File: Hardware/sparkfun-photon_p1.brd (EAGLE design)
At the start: 68.6 x 53.3 mm, 44 parts, among them U1 WM-N-BM-14

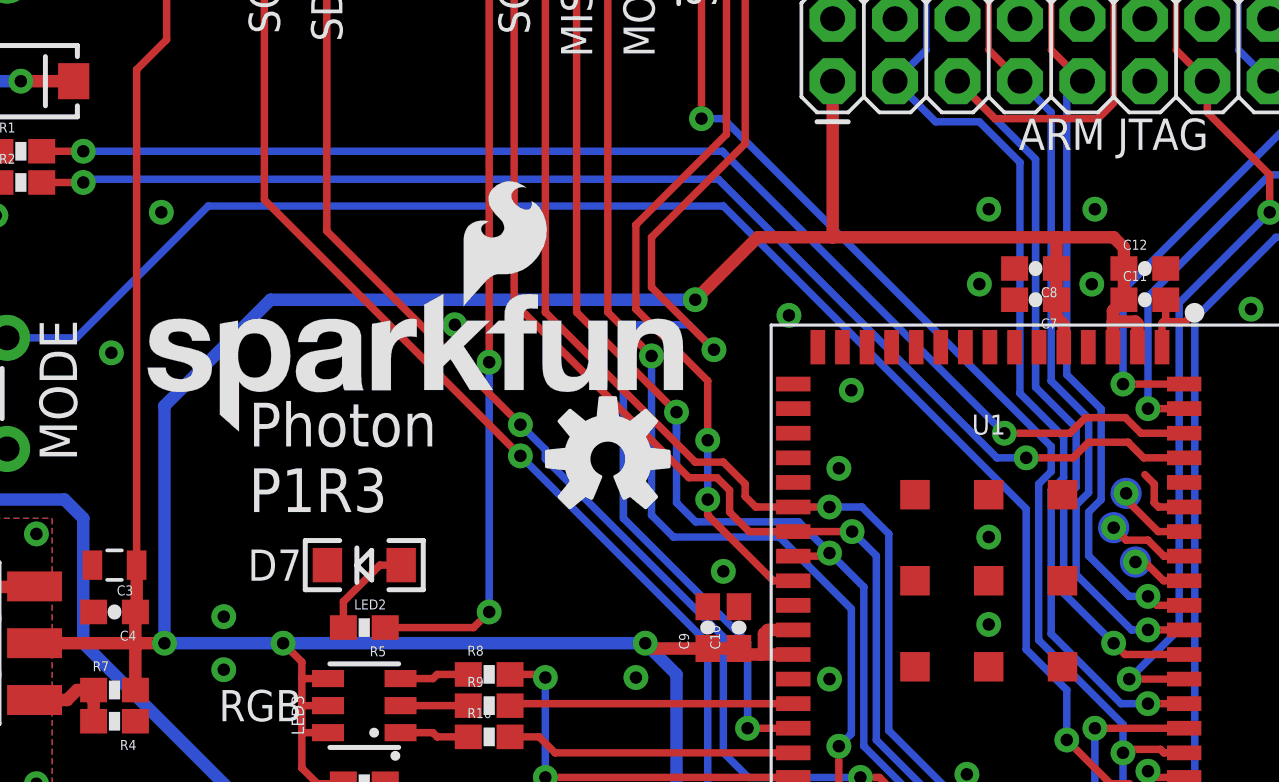
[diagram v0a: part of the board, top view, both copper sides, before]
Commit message: Moving a few vias for a more complete ground plane. Adjusting some silk.
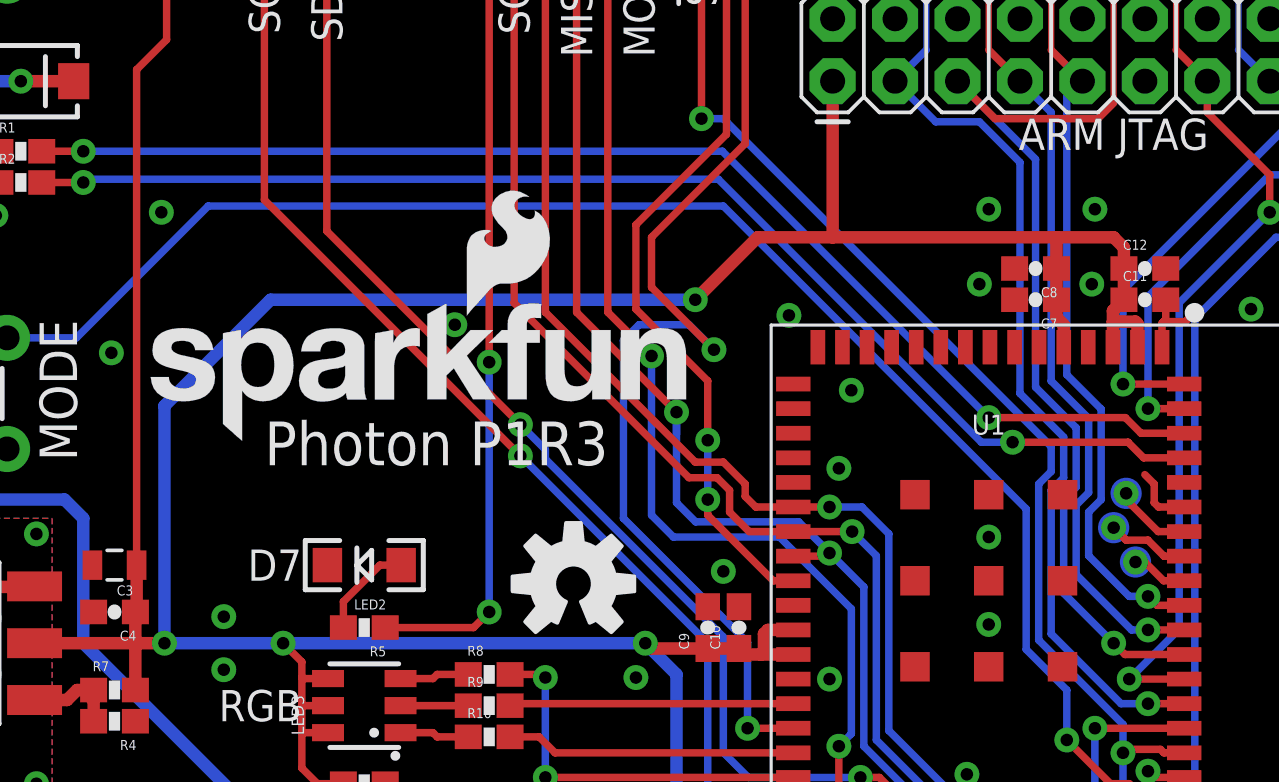
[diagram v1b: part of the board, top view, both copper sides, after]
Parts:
- moved LOGO1 5.27 mm to (31.4, 21.5)
- moved LOGO2 0.40 mm to (13.5, 27.2)
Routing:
- net MCU_USB_D-: track 51.7 -> 51.2 mm
- net MCU_USB_D+: track 51.7 -> 51.2 mm
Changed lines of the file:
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@@
 <layer number="47" name="Measures" color="7" fill="1" visible="no" active="yes"/>
 <layer number="48" name="Document" color="7" fill="1" visible="no" active="yes"/>
-<layer number="49" name="Reference" color="7" fill="1" visible="yes" active="yes"/>
+<layer number="49" name="Reference" color="7" fill="1" visible="no" active="yes"/>
 <layer number="50" name="dxf" color="7" fill="1" visible="no" active="no"/>
 <layer number="51" name="tDocu" color="6" fill="1" visible="yes" active="yes"/>
@@
 <text x="20.32" y="22.225" size="1.27" layer="21" font="vector" ratio="15" rot="R180" align="center-left">D7</text>
 <text x="20.32" y="10.795" size="1.27" layer="21" font="vector" ratio="15" rot="R180" align="center-left">POWER</text>
-<text x="18.161" y="28.829" size="1.778" layer="21" font="vector" ratio="15" align="top-left">Photon
-P1R3</text>
+<text x="18.796" y="28.067" size="1.778" layer="21" font="vector" ratio="15" align="top-left">Photon P1R3</text>
 <text x="9.652" y="29.337" size="1.524" layer="21" font="vector" ratio="15" rot="R90" align="top-center">MODE</text>
 <text x="9.652" y="48.387" size="1.524" layer="21" font="vector" ratio="15" rot="R90" align="top-center">RESET</text>
@@
 <attribute name="PROD_ID" value="CAP-00810" x="54.61" y="34.29" size="1.778" layer="27" font="vector" ratio="15" display="off"/>
 </element>
-<element name="LOGO2" library="SparkFun-Aesthetics" package="SFE_LOGO_NAME_FLAME_.2" value="SFE_LOGO_NAME_FLAME.2_INCH" x="13.335" y="27.559"/>
-<element name="LOGO1" library="SparkFun-Aesthetics" package="OSHW-LOGO-M" value="OSHW-LOGOM" x="32.766" y="26.543"/>
+<element name="LOGO2" library="SparkFun-Aesthetics" package="SFE_LOGO_NAME_FLAME_.2" value="SFE_LOGO_NAME_FLAME.2_INCH" x="13.462" y="27.178"/>
+<element name="LOGO1" library="SparkFun-Aesthetics" package="OSHW-LOGO-M" value="OSHW-LOGOM" x="31.369" y="21.463"/>
 <element name="U1" library="sparkfun_photon_temp" package="WM-N-BM-14" value="WM-N-BM-14" x="48.26" y="21.59">
 <attribute name="PROD_ID" value="IC-12589" x="48.26" y="21.59" size="1.778" layer="27" font="vector" ratio="15" display="off"/>
@@
 <wire x1="9.74" y1="39.06" x2="11.43" y2="39.06" width="0.3048" layer="1"/>
 <via x="11.43" y="39.06" extent="1-16" drill="0.508"/>
-<via x="48.895" y="27.59" extent="1-16" drill="0.508"/>
+<via x="48.26" y="28.225" extent="1-16" drill="0.508"/>
 <wire x1="11.43" y1="39.06" x2="37.425" y2="39.06" width="0.3048" layer="16"/>
-<wire x1="48.895" y1="27.59" x2="37.425" y2="39.06" width="0.3048" layer="16"/>
+<wire x1="48.26" y1="28.225" x2="37.425" y2="39.06" width="0.3048" layer="16"/>
 <wire x1="56.21" y1="27.59" x2="54.452" y2="27.59" width="0.3048" layer="1"/>
 <wire x1="54.452" y1="27.59" x2="53.817" y2="28.225" width="0.3048" layer="1"/>
-<wire x1="53.817" y1="28.225" x2="52.197" y2="28.225" width="0.3048" layer="1"/>
-<wire x1="52.197" y1="28.225" x2="51.562" y2="27.59" width="0.3048" layer="1"/>
-<wire x1="51.562" y1="27.59" x2="48.895" y2="27.59" width="0.3048" layer="1"/>
+<wire x1="48.26" y1="28.225" x2="53.817" y2="28.225" width="0.3048" layer="1"/>
 </signal>
 <signal name="MCU_USB_D+">
@@
 <wire x1="9.74" y1="37.79" x2="11.43" y2="37.79" width="0.3048" layer="1"/>
 <via x="11.43" y="37.79" extent="1-16" drill="0.508"/>
-<via x="49.784" y="26.59" extent="1-16" drill="0.508"/>
-<wire x1="48.594" y1="26.59" x2="37.2618" y2="37.9222" width="0.3048" layer="16"/>
 <wire x1="37.2618" y1="37.9222" x2="11.5622" y2="37.9222" width="0.3048" layer="16"/>
 <wire x1="11.5622" y1="37.9222" x2="11.43" y2="37.79" width="0.3048" layer="16"/>
 <wire x1="56.21" y1="26.59" x2="54.563" y2="26.59" width="0.3048" layer="1"/>
 <wire x1="54.563" y1="26.59" x2="53.928" y2="27.225" width="0.3048" layer="1"/>
-<wire x1="49.784" y1="26.59" x2="48.594" y2="26.59" width="0.3048" layer="16"/>
-<wire x1="53.928" y1="27.225" x2="52.324" y2="27.225" width="0.3048" layer="1"/>
-<wire x1="52.324" y1="27.225" x2="51.689" y2="26.59" width="0.3048" layer="1"/>
-<wire x1="51.689" y1="26.59" x2="49.784" y2="26.59" width="0.3048" layer="1"/>
+<via x="49.229" y="27.225" extent="1-16" drill="0.508"/>
+<wire x1="49.229" y1="27.225" x2="53.928" y2="27.225" width="0.3048" layer="1"/>
+<wire x1="49.229" y1="27.225" x2="47.959" y2="27.225" width="0.3048" layer="16"/>
+<wire x1="47.959" y1="27.225" x2="37.2618" y2="37.9222" width="0.3048" layer="16"/>
 </signal>
 <signal name="VUSB">
@@
 </board>
 </drawing>
-<compatibility>
-<note version="6.3" minversion="6.2.2" severity="warning">
-Since Version 6.2.2 text objects can contain more than one line,
-which will not be processed correctly with this version.
-</note>
-</compatibility>
 </eagle>

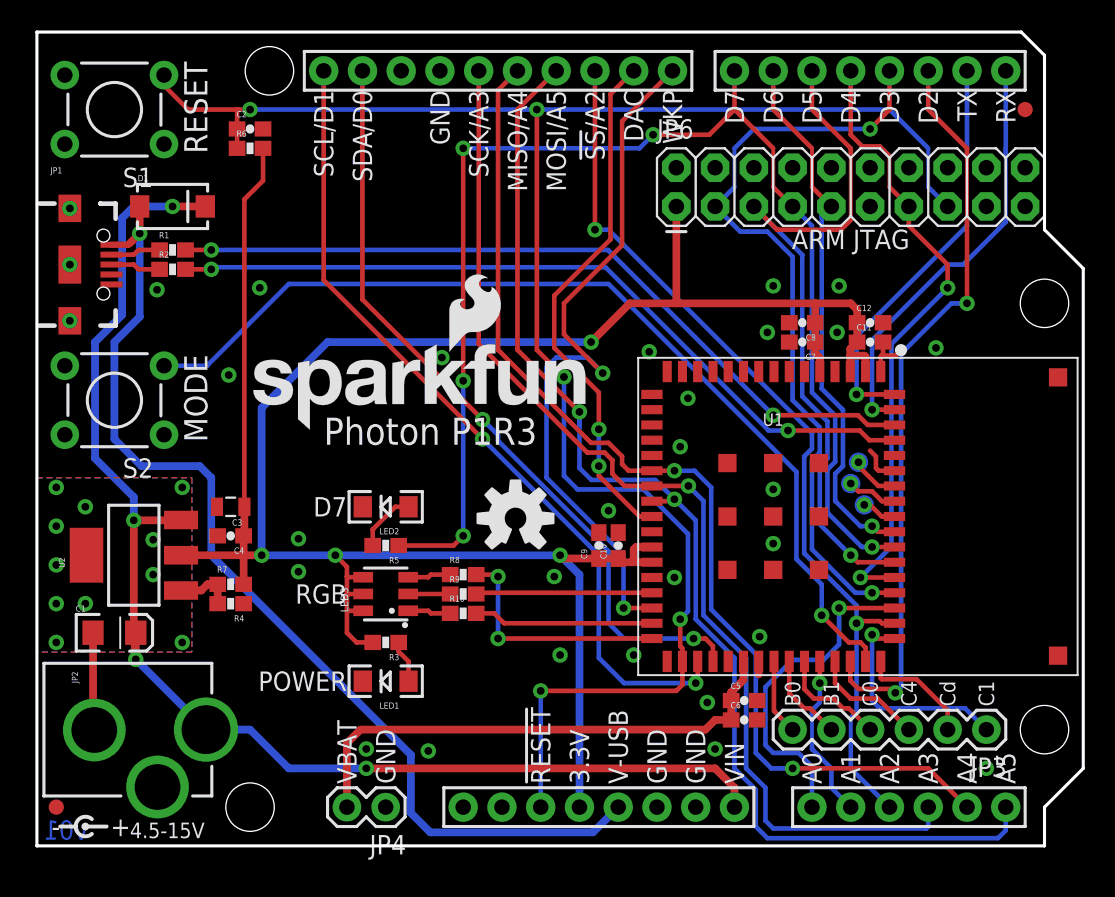
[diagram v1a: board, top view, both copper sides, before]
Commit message: Swap WKP & RGB red signals. Add tp's to WL JTAG.
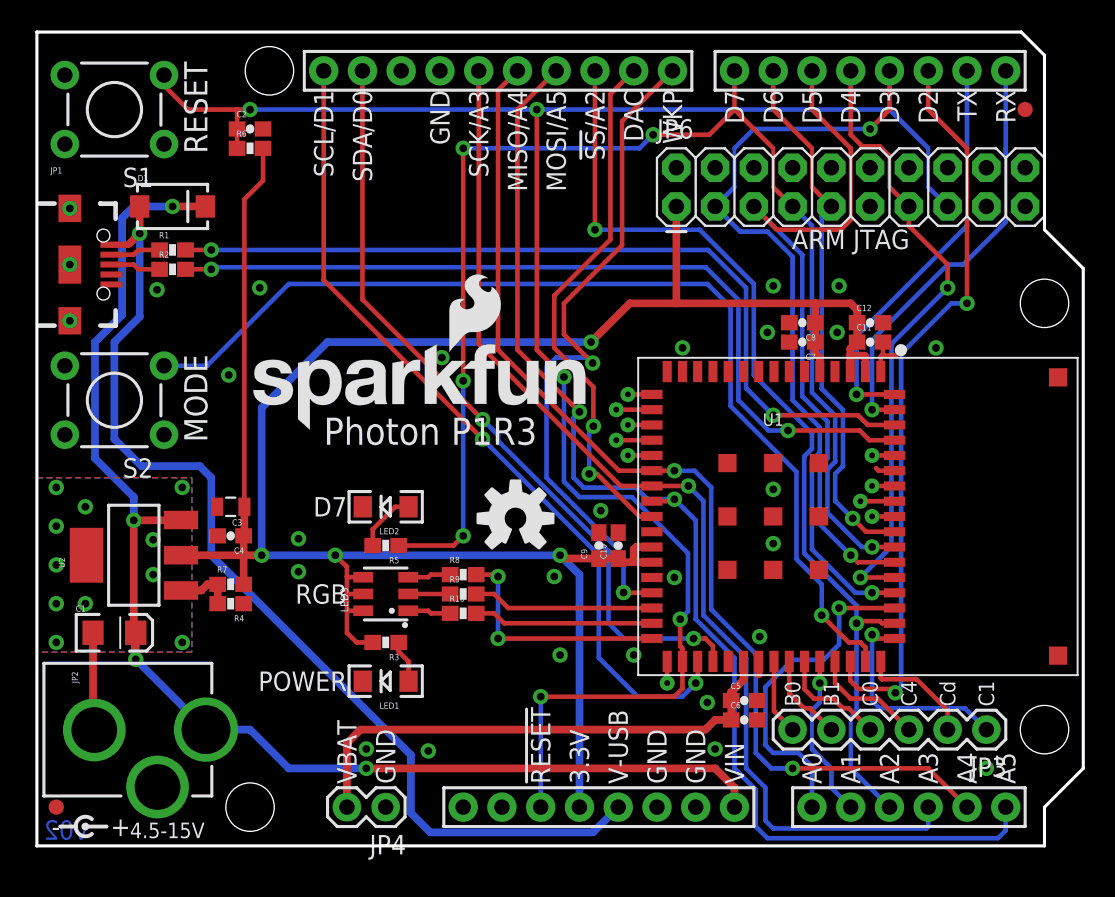
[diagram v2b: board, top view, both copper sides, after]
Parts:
- added TP10, TP4, TP5, TP6, TP7, TP8, TP9: TEST-POINTTP_15TH_THRU, SparkFun-Passives:TP_15TH
- TP1, TP2, TP3: value TEST-POINT3X5 -> TEST-POINTTP_15TH_THRU; device SparkFun-Passives:PAD.03X.05 -> SparkFun-Passives:TP_15TH
- moved TP1 1.79 mm to (54.7, 23.6), flipped to the top
- moved TP3 1.32 mm to (54.0, 22.6), flipped to the top
- moved TP2 0.92 mm to (54.7, 21.6), flipped to the top
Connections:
- net N$1 renamed BTCX_TXCONF
- net N$2 renamed BTCX_STATUS
- net N$8 renamed BTCX_RF_ACTIVE
- new net N$1: TP10.P$1, U1.33
- new net WL_JTAG_TCK: TP5.P$1, U1.17
- new net WL_JTAG_TDI: TP4.P$1, U1.16
- new net WL_JTAG_TDO: TP8.P$1, U1.20
- new net WL_JTAG_TMS: TP7.P$1, U1.19
- new net WL_JTAG_TRST: TP6.P$1, U1.18
- new net WL_SLEEP_CLK: TP9.P$1, U1.60
- net RGB_RED: now also U1.30; no longer U1.29
- net WKP: now also U1.29; no longer U1.30
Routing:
- net MCU_USB_D+: track 51.2 -> 55.1 mm
- net MCU_USB_D-: track 51.2 -> 55.1 mm
- net !MODE: track 63.5 -> 67.3 mm
- net A2: track 60.1 -> 63.6 mm
- net WKP: track 47.9 -> 45.0 mm
- net WL_JTAG_TMS: track 0.00 -> 2.34 mm
- net WL_JTAG_TCK: track 0.00 -> 2.34 mm
- net BTCX_TXCONF: track 3.16 -> 1.47 mm, vias 1 -> 0
- net WL_JTAG_TRST: track 0.00 -> 1.58 mm
- net WL_JTAG_TDO: track 0.00 -> 1.58 mm
- net WL_JTAG_TDI: track 0.00 -> 1.58 mm
- net WL_SLEEP_CLK: track 0.00 -> 1.47 mm
- net N$1: track 0.00 -> 1.42 mm
- net GND: track 13.1 -> 11.8 mm, vias 30 -> 28
- net BTCX_RF_ACTIVE: track 3.35 -> 2.23 mm, vias 1 -> 0
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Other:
- board text added: "BTCX-RF_ACT"
- board text added: "BTCX-STAT"
- board text added: "BTCX-TXCONF"
- board text added: "WL-SLP-CLK"
- board text added: "WL-TCK"
- board text added: "WL-TDI"
- board text added: "WL-TDO"
- board text added: "WL-TMS"
- board text added: "WL-TRST"
- board text added: "v02"
- board text removed: "v01"

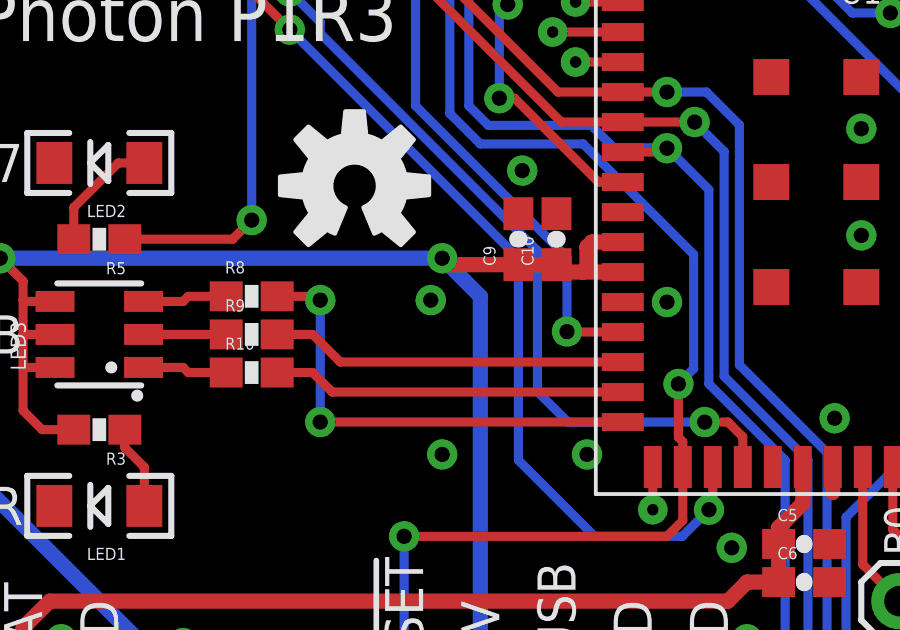
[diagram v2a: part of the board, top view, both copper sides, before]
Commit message: Swapping PA1 and PA0 (Red RGB and WKP pins).
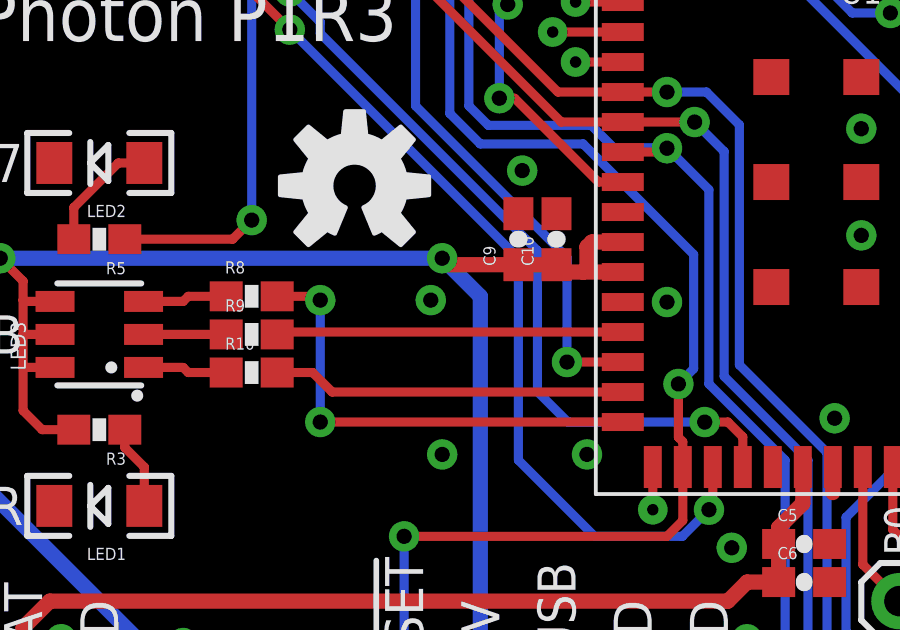
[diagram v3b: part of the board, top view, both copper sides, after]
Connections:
- net A3 renamed A3/SPI_SCK
- net A4 renamed A4/SPI_MISO
- net A5 renamed A5/SPI_MOSI
- net RGB_RED: now also U1.29; no longer U1.30
- net WKP: now also U1.30; no longer U1.29
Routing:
- net WKP: track 45.0 -> 46.0 mm
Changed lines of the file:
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@@
 <layer number="28" name="bValues" color="7" fill="1" visible="no" active="yes"/>
 <layer number="29" name="tStop" color="7" fill="3" visible="no" active="yes"/>
-<layer number="30" name="bStop" color="7" fill="6" visible="yes" active="yes"/>
+<layer number="30" name="bStop" color="7" fill="6" visible="no" active="yes"/>
 <layer number="31" name="tCream" color="7" fill="4" visible="no" active="yes"/>
 <layer number="32" name="bCream" color="7" fill="5" visible="no" active="yes"/>
@@
 <layer number="47" name="Measures" color="7" fill="1" visible="no" active="yes"/>
 <layer number="48" name="Document" color="7" fill="1" visible="no" active="yes"/>
-<layer number="49" name="Reference" color="7" fill="1" visible="yes" active="yes"/>
+<layer number="49" name="Reference" color="7" fill="1" visible="no" active="yes"/>
 <layer number="50" name="dxf" color="7" fill="1" visible="no" active="no"/>
 <layer number="51" name="tDocu" color="6" fill="1" visible="yes" active="yes"/>
@@
 <signal name="RGB_RED">
 <contactref element="R9" pad="2"/>
-<contactref element="U1" pad="30"/>
-<wire x1="40.31" y1="15.59" x2="30.892" y2="15.59" width="0.3048" layer="1"/>
-<wire x1="30.892" y1="15.59" x2="29.972" y2="16.51" width="0.3048" layer="1"/>
-<wire x1="28.79" y1="16.51" x2="29.972" y2="16.51" width="0.3048" layer="1"/>
+<contactref element="U1" pad="29"/>
+<wire x1="40.31" y1="16.59" x2="28.87" y2="16.59" width="0.3048" layer="1"/>
+<wire x1="28.87" y1="16.59" x2="28.79" y2="16.51" width="0.3048" layer="1"/>
 </signal>
 <signal name="RGB_GREEN">
@@
 <wire x1="36.4744" y1="27.5082" x2="36.4744" y2="30.0736" width="0.3048" layer="1"/>
 </signal>
-<signal name="A5">
+<signal name="A5/SPI_MOSI">
 <contactref element="JP5" pad="A5"/>
 <contactref element="JP5" pad="D11"/>
@@
 <wire x1="35.179" y1="28.067" x2="35.56" y2="28.448" width="0.3048" layer="16"/>
 </signal>
-<signal name="A3">
+<signal name="A3/SPI_SCK">
 <contactref element="JP5" pad="A3"/>
 <contactref element="JP5" pad="D13"/>
@@
 <wire x1="40.31" y1="23.59" x2="38.259" y2="23.59" width="0.3048" layer="1"/>
 </signal>
-<signal name="A4">
+<signal name="A4/SPI_MISO">
 <contactref element="JP5" pad="A4"/>
 <contactref element="JP5" pad="D12"/>
@@
 </signal>
 <signal name="WKP">
-<via x="38.45" y="16.606" extent="1-16" drill="0.508"/>
+<via x="38.45" y="15.59" extent="1-16" drill="0.508"/>
 <wire x1="38.45" y1="19.081" x2="33.401" y2="24.13" width="0.3048" layer="16"/>
-<wire x1="38.45" y1="16.606" x2="38.45" y2="19.081" width="0.3048" layer="16"/>
+<wire x1="38.45" y1="15.59" x2="38.45" y2="19.081" width="0.3048" layer="16"/>
 <contactref element="JP5" pad="D8"/>
 <wire x1="33.401" y1="24.13" x2="33.401" y2="31.369" width="0.3048" layer="16"/>
@@
 <wire x1="34.036" y1="32.004" x2="36.068" y2="32.004" width="0.3048" layer="16"/>
 <wire x1="36.068" y1="32.004" x2="36.4236" y2="31.6484" width="0.3048" layer="16"/>
-<contactref element="U1" pad="29"/>
-<wire x1="40.31" y1="16.59" x2="38.466" y2="16.59" width="0.3048" layer="1"/>
-<wire x1="38.466" y1="16.59" x2="38.45" y2="16.606" width="0.3048" layer="1"/>
+<contactref element="U1" pad="30"/>
+<wire x1="40.31" y1="15.59" x2="38.45" y2="15.59" width="0.3048" layer="1"/>
 </signal>
 <signal name="VBAT">
